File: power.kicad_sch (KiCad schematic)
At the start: 95 parts, among them Q10 2NPN, Q3 PMOS, Q4 PMOS, Q5 PMOS, Q6 PMOS, Q7 2NPN, Q9 2PNP, U21 TPS62410, U22 LDO-2V5, U28 AP22652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

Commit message: Use consistent footprints for 0402 and 0201 diodes
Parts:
- D11, D16, D17: footprint praline:DFN1006-2 -> praline:TSLP-2-19
- L10: Part Number NRS4018T4R7MDGJ -> LSXND4040TKL4R7MDG; Substitution NRG4026T4R7M -> NRS4018T4R7MDGJ, LLXND4040TKL4R7MDG, NRS4018T4R7MDGJ
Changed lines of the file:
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@@
 			)
 		)
-		(property "Footprint" "praline:DFN1006-2"
+		(property "Footprint" "praline:TSLP-2-19"
 			(at 31.75 50.8 0)
 			(effects
@@
 			)
 		)
-		(property "Footprint" "praline:DFN1006-2"
+		(property "Footprint" "praline:TSLP-2-19"
 			(at 31.75 92.71 0)
 			(effects
@@
 			)
 		)
-		(property "Part Number" "NRS4018T4R7MDGJ"
+		(property "Part Number" "LSXND4040TKL4R7MDG"
 			(at 166.37 35.56 90)
 			(effects
@@
 			)
 		)
-		(property "Substitution" "NRG4026T4R7M"
+		(property "Substitution" "NRS4018T4R7MDGJ, LLXND4040TKL4R7MDG, NRS4018T4R7MDGJ"
 			(at 166.37 35.56 0)
 			(effects
@@
 			)
 		)
-		(property "Footprint" "praline:DFN1006-2"
+		(property "Footprint" "praline:TSLP-2-19"
 			(at 91.44 80.01 0)
 			(effects

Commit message: Correct component metadata
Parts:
- R58, R70: Part Number RC0402JR-07820KL -> RC0402FR-07820KL
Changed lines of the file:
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@@
 			)
 		)
-		(property "Description" "RES 820K OHM 5% 1/16W 0402"
+		(property "Description" "RES 820K OHM 1% 1/16W 0402"
 			(at 68.58 40.64 0)
 			(effects
@@
 			)
 		)
-		(property "Part Number" "RC0402JR-07820KL"
+		(property "Part Number" "RC0402FR-07820KL"
 			(at 68.58 40.64 0)
 			(effects
@@
 			)
 		)
-		(property "Description" "RES 820K OHM 5% 1/16W 0402"
+		(property "Description" "RES 820K OHM 1% 1/16W 0402"
 			(at 68.58 82.55 0)
 			(effects
@@
 			)
 		)
-		(property "Part Number" "RC0402JR-07820KL"
+		(property "Part Number" "RC0402FR-07820KL"
 			(at 68.58 82.55 0)
 			(effects

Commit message: Replace mixer compensation amps with single BGB741
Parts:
- R77, R78: footprint Resistor_SMD:R_0402_1005Metric -> Resistor_SMD:R_0201_0603Metric; Part Number RC0402JR-072K2L -> RC0201JR-072K2L
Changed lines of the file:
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@@
 			)
 		)
-		(property "Footprint" "Resistor_SMD:R_0402_1005Metric"
+		(property "Footprint" "Resistor_SMD:R_0201_0603Metric"
 			(at 54.61 102.108 90)
 			(effects
@@
 			)
 		)
-		(property "Description" "RES 2.2K OHM 5% 1/16W 0402"
+		(property "Description" "RES 2.2K OHM 5% 1/20W 0201"
 			(at 54.61 100.33 0)
 			(effects
@@
 			)
 		)
-		(property "Part Number" "RC0402JR-072K2L"
+		(property "Part Number" "RC0201JR-072K2L"
 			(at 54.61 100.33 0)
 			(effects
@@
 			)
 		)
-		(property "Footprint" "Resistor_SMD:R_0402_1005Metric"
+		(property "Footprint" "Resistor_SMD:R_0201_0603Metric"
 			(at 54.61 60.198 90)
 			(effects
@@
 			)
 		)
-		(property "Description" "RES 2.2K OHM 5% 1/16W 0402"
+		(property "Description" "RES 2.2K OHM 5% 1/20W 0201"
 			(at 54.61 58.42 0)
 			(effects
@@
 			)
 		)
-		(property "Part Number" "RC0402JR-072K2L"
+		(property "Part Number" "RC0201JR-072K2L"
 			(at 54.61 58.42 0)
 			(effects

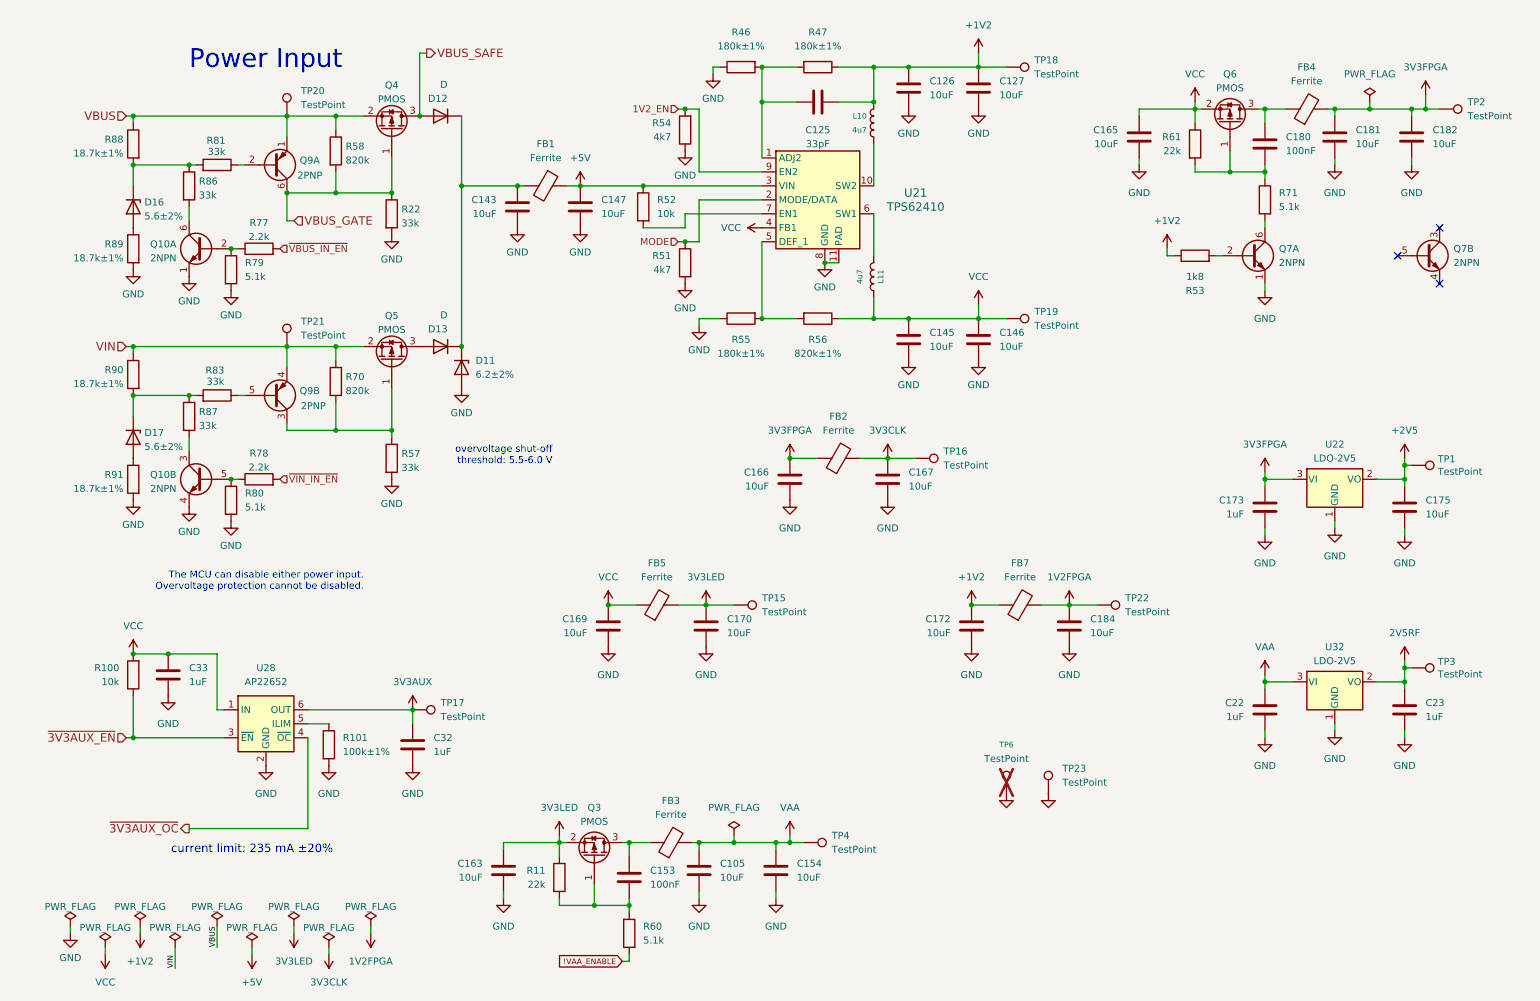
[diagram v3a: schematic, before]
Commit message: Standardize component Value fields
Use Tolerance field instead of expressing tolerance in Value field
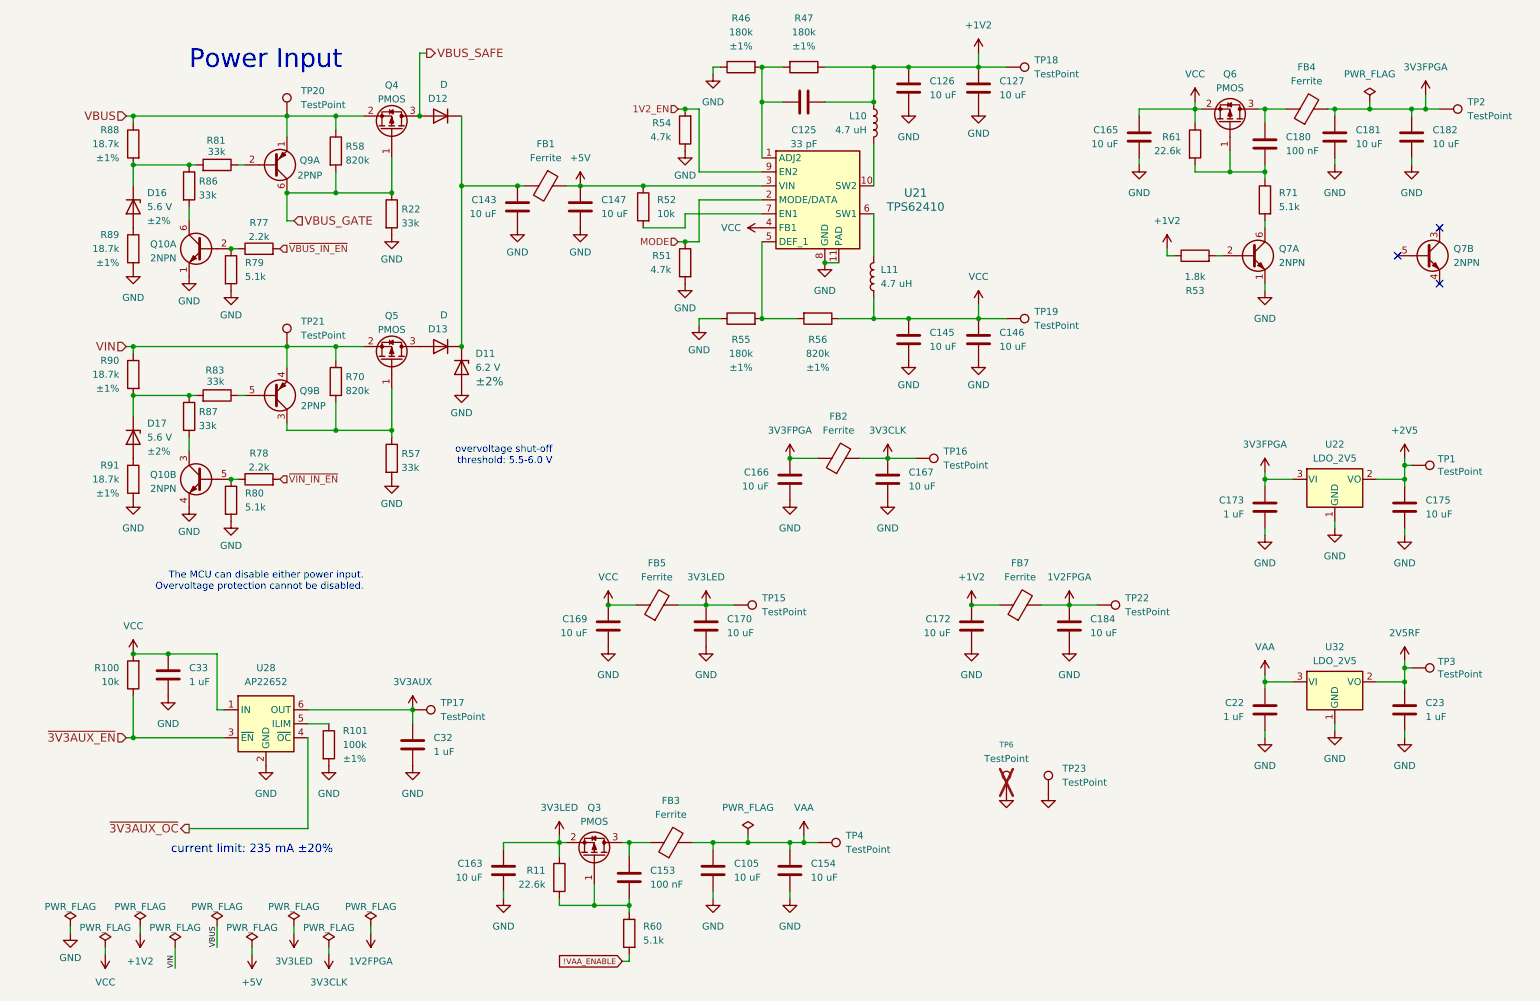
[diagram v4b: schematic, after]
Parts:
- C105, C126, C127, C143, C145, C146, C147, C154, C163, C165, C166, C167, C169, C170, C172, C175, C181, C182, C184: value 10uF -> 10 uF
- C125: value 33pF -> 33 pF
- C153, C180: value 100nF -> 100 nF
- C173, C22, C23, C32, C33: value 1uF -> 1 uF
- D11: value 6.2±2% -> 6.2 V; Tolerance (none) -> ±2%
- D16, D17: value 5.6±2% -> 5.6 V; Tolerance (none) -> ±2%
- L10, L11: value 4u7 -> 4.7 uH
- R101: value 100k±1% -> 100k; Tolerance (none) -> ±1%
- R11, R61: value 22k -> 22.6k
- R46, R47, R55: value 180k±1% -> 180k; Tolerance (none) -> ±1%
- R51, R54: value 4k7 -> 4.7k
- R53: value 1k8 -> 1.8k
- R56: value 820k±1% -> 820k; Tolerance (none) -> ±1%
- R88, R89, R90, R91: value 18.7k±1% -> 18.7k; Tolerance (none) -> ±1%
- U22, U32: value LDO-2V5 -> LDO_2V5
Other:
- moved on the sheet: C105, C125, C154, L10, R47, TP4

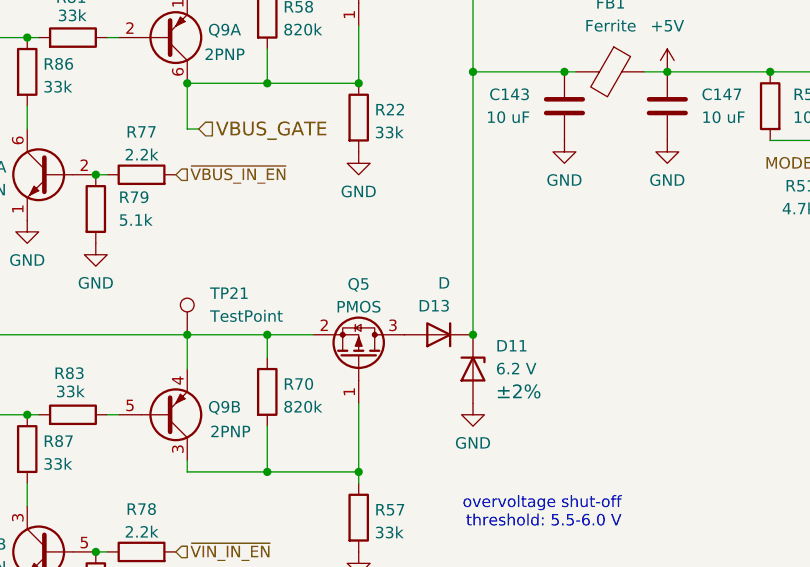
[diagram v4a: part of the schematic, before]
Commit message: Change D13 to PMEG4010ESBYL
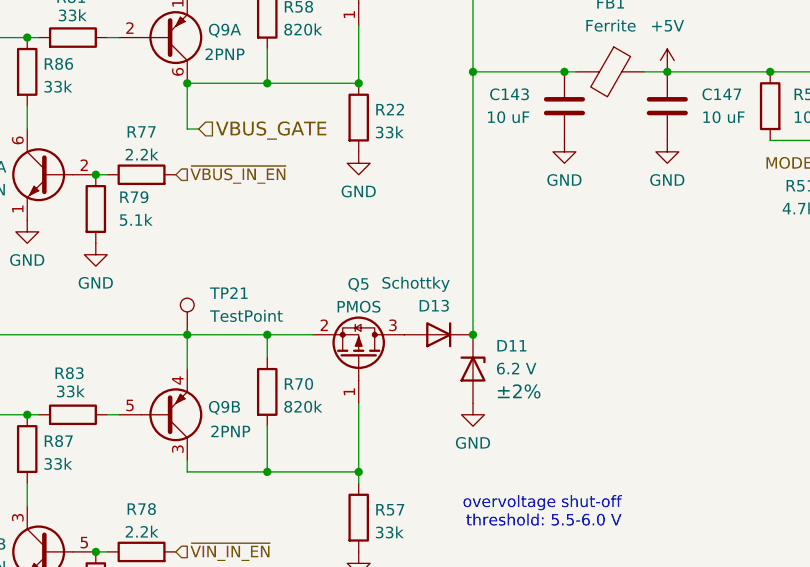
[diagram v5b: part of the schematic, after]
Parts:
- D13: value D -> Schottky; footprint praline:D_SOD-123FL -> praline:TSLP-2-19; Manufacturer Yangzhou Yangjie -> Nexperia; Part Number U1D -> PMEG4010ESBYL
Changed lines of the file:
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@@
 			)
 		)
-		(property "Value" "D"
+		(property "Value" "Schottky"
 			(at 88.9 70.485 0)
 			(effects
@@
 			)
 		)
-		(property "Footprint" "praline:D_SOD-123FL"
+		(property "Footprint" "praline:TSLP-2-19"
 			(at 87.63 76.2 0)
 			(effects
@@
 			)
 		)
-		(property "Datasheet" "https://www.21yangjie.com/pdf/zlqj/ckfhejg/U1A%20THRU%20U1J.pdf"
+		(property "Datasheet" "~"
 			(at 87.63 76.2 0)
 			(effects
@@
 			)
 		)
-		(property "Description" "SOD-123FL 200V 1.0A  Diodes Rec"
+		(property "Description" "DIODE SCHOTTKY 40V 1A DSN1006-2"
 			(at 87.63 76.2 0)
 			(effects
@@
 			)
 		)
-		(property "Manufacturer" "Yangzhou Yangjie"
+		(property "Manufacturer" "Nexperia"
 			(at 87.63 76.2 0)
 			(effects
@@
 			)
 		)
-		(property "Part Number" "U1D"
+		(property "Part Number" "PMEG4010ESBYL"
 			(at 87.63 76.2 0)
 			(effects

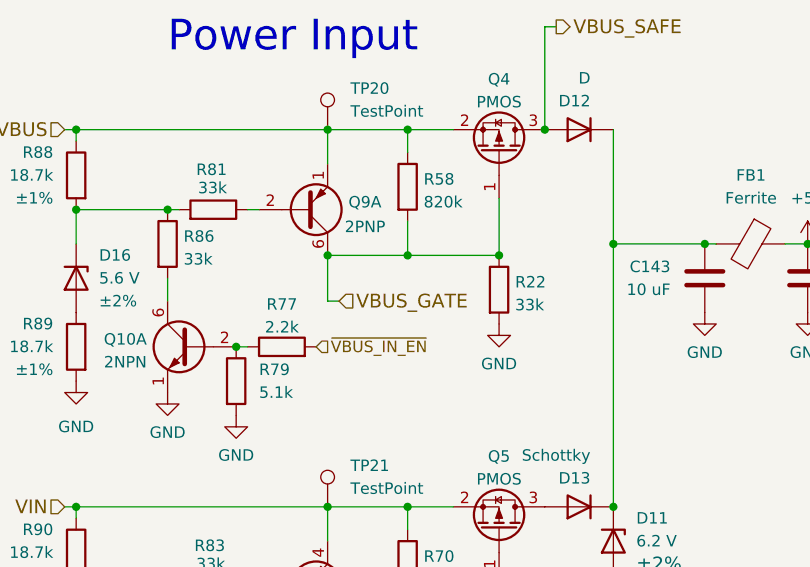
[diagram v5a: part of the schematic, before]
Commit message: Use Type-C power instead of Type-C controller
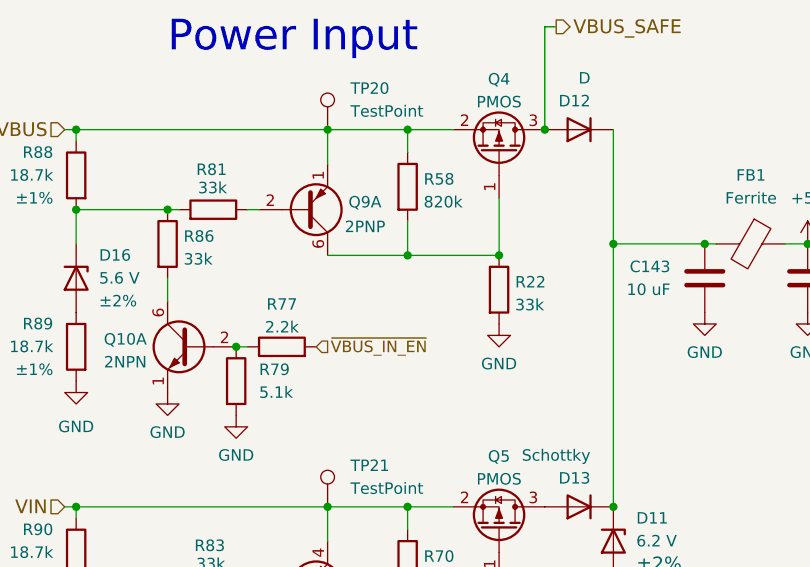
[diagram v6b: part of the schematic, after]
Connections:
- net VBUS_GATE: no longer names the net of Q4.1 (G), Q9.6 (C1), R22.1, R58.2
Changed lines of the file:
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@@
-		(color 0 0 0 0)
-	)
-	(junction
-		(at 59.69 48.26)
-		(diameter 0)
 		(color 0 0 0 0)
 	)
@@
 	(wire
 		(pts
-			(xy 59.69 53.34) (xy 60.96 53.34)
-		)
-		(stroke
-			(width 0)
-			(type default)
-		)
-	)
-	(wire
-		(pts
 			(xy 99.06 166.37) (xy 99.06 167.64)
 		)
@@
 		(pts
 			(xy 121.92 168.91) (xy 121.92 166.37)
-		)
-		(stroke
-			(width 0)
-			(type default)
-		)
-	)
-	(wire
-		(pts
-			(xy 59.69 48.26) (xy 59.69 53.34)
 		)
 		(stroke
@@
 		)
 	)
-	(hierarchical_label "VBUS_GATE"
-		(shape input)
-		(at 60.96 53.34 0)
-		(effects
-			(font
-				(size 1.524 1.524)
-			)
-			(justify left)
-		)
-	)

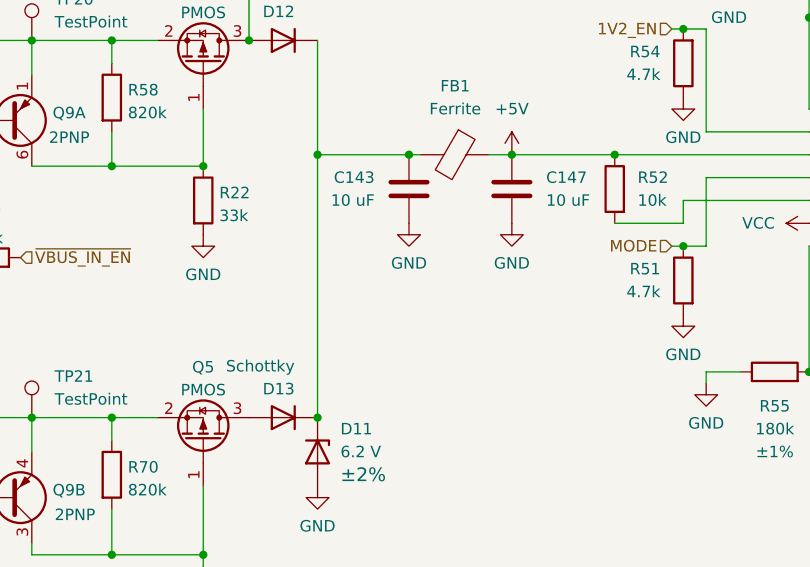
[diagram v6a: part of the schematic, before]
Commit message: Update component selections
- Change C143, C147 to 22 uF CL21A226MAYNNNE
- Change VIN diode D13 to 0 ohm resistor
- Change R29 to 100 ohm
- Change limiter Schottky D15 to JDH2S02SL,L3F
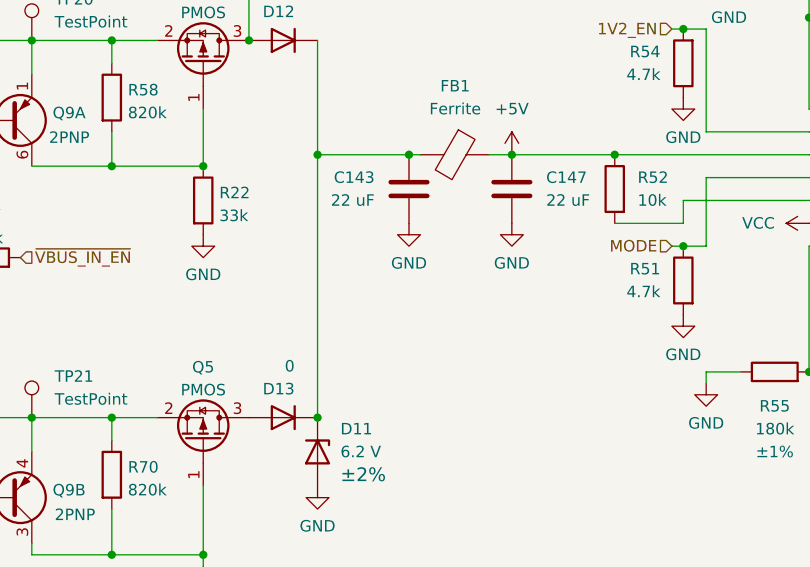
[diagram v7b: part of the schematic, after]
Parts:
- C143, C147: value 10 uF -> 22 uF; Part Number CL21A106KOQNNNE -> CL21A226MAYNNNE
- D13: value Schottky -> 0; Manufacturer Nexperia -> Yageo; Part Number PMEG4010ESBYL -> RC0201JR-070RL
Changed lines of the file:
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@@
 			)
 		)
-		(property "Value" "Schottky"
+		(property "Value" "0"
 			(at 88.9 70.485 0)
 			(effects
@@
 			)
 		)
-		(property "Description" "DIODE SCHOTTKY 40V 1A DSN1006-2"
+		(property "Description" "RES 0 OHM JUMPER 1/20W 0201"
 			(at 87.63 76.2 0)
 			(effects
@@
 			)
 		)
-		(property "Manufacturer" "Nexperia"
+		(property "Manufacturer" "Yageo"
+			(at 87.63 76.2 0)
+			(effects
+				(font
+					(size 1.27 1.27)
+				)
+				(hide yes)
+			)
+		)
+		(property "Part Number" "RC0201JR-070RL"
 			(at 87.63 76.2 0)
 			(effects
@@
 			)
 		)
-		(property "Part Number" "PMEG4010ESBYL"
+		(property "Tolerance" ""
 			(at 87.63 76.2 0)
 			(effects
@@
 			)
 		)
-		(property "Value" "10 uF"
+		(property "Value" "22 uF"
 			(at 97.79 52.0699 0)
 			(effects
@@
 			)
 		)
-		(property "Description" "CAP CER 10UF 16V X5R 0805"
+		(property "Description" "CAP CER 22UF 25V X5R 0805"
 			(at 101.6 50.8 0)
 			(effects
@@
 			)
 		)
-		(property "Part Number" "CL21A106KOQNNNE"
+		(property "Part Number" "CL21A226MAYNNNE"
 			(at 101.6 50.8 0)
 			(effects
@@
 			)
 		)
-		(property "Value" "10 uF"
+		(property "Value" "22 uF"
 			(at 116.84 52.0699 0)
 			(effects
@@
 			)
 		)
-		(property "Description" "CAP CER 10UF 16V X5R 0805"
+		(property "Description" "CAP CER 22UF 25V X5R 0805"
 			(at 113.03 50.8 0)
 			(effects
@@
 			)
 		)
-		(property "Part Number" "CL21A106KOQNNNE"
+		(property "Part Number" "CL21A226MAYNNNE"
 			(at 113.03 50.8 0)
 			(effects
